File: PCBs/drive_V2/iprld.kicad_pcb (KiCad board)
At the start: 2 copper layers, 100 x 100 mm, 87 parts, among them IC1 W25Q16JVUXIQ_TR, IC2 ADS1115IDGSR, J1 TYPE-C-31-M-12, U1 AMS1117-3.3, U11 4N35, U12 4N35, U13 4N35, U14 4N35, U2 ESP32-S3, U3 4N35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

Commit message: fixed merge issues
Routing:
- net GND: track 251.2 -> 248.9 mm, vias 45 -> 44

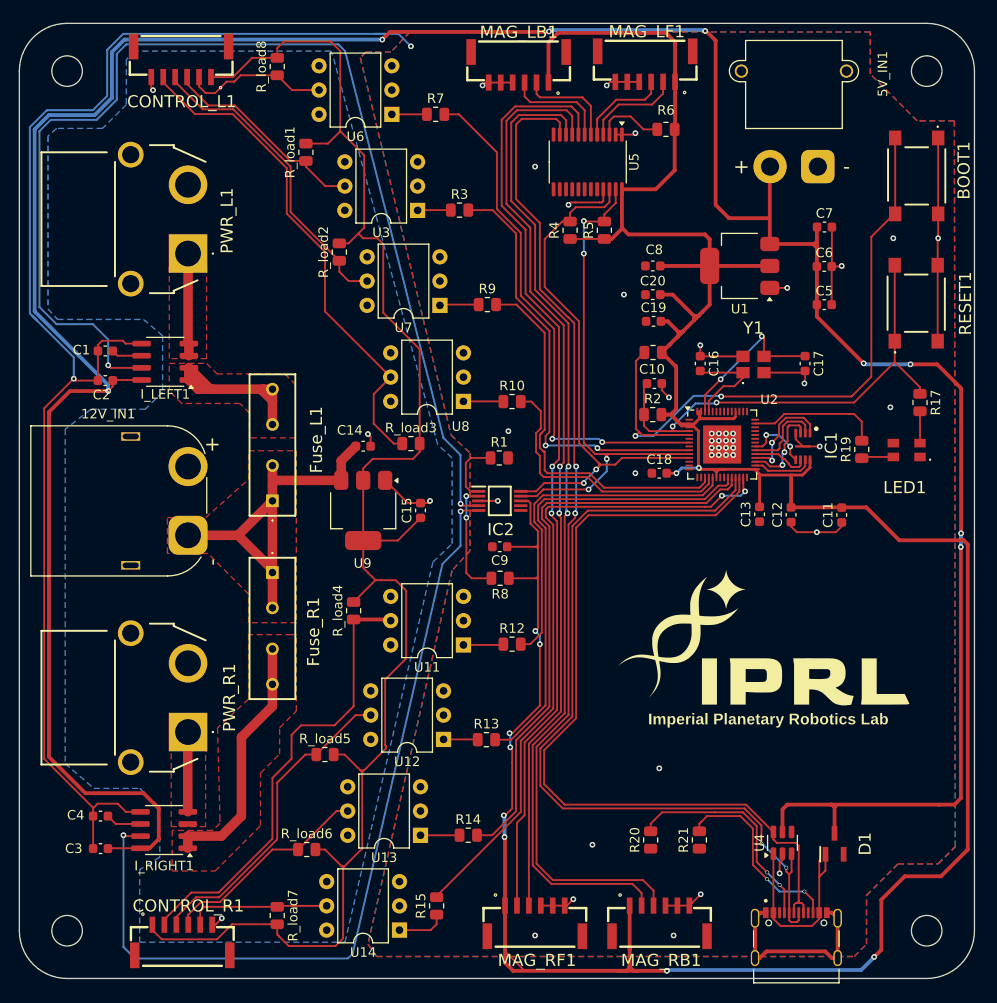
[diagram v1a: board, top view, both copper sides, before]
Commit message: added potential divider for I_OUT signals
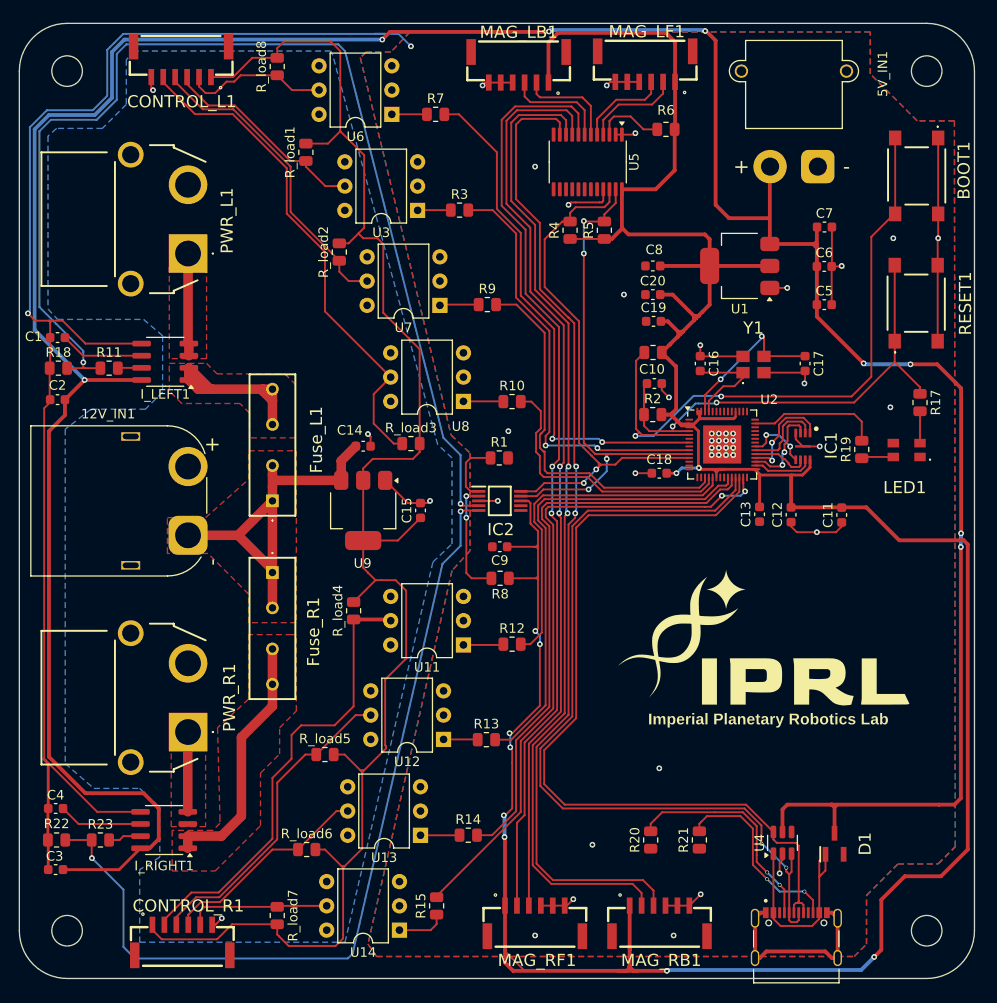
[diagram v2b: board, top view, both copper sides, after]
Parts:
- added R11: 5.1k, Resistor_SMD:R_0805_2012Metric, F.Cu at (9.40, 36.1)
- added R18: 10k, Resistor_SMD:R_0805_2012Metric, F.Cu at (4.09, 36.1)
- added R22: 10k, Resistor_SMD:R_0805_2012Metric, F.Cu at (3.90, 85.5)
- added R23: 5.1k, Resistor_SMD:R_0805_2012Metric, F.Cu at (8.49, 85.5)
- moved C2 5.39 mm to (4.00, 39.4)
- moved C1 5.19 mm to (4.00, 32.9)
- moved C3 5.19 mm to (3.80, 88.6)
- moved C4 4.77 mm to (3.80, 82.2)
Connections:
- IC1 pad 2: /SPIQ -> /SPID
- I_LEFT1 pad 7: /I_OUT_L -> Net-(I_LEFT1-VIOUT)
- I_RIGHT1 pad 7: /I_OUT_R -> Net-(I_RIGHT1-VIOUT)
- U2 pad 34: /SPIQ -> /SPID
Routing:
- net /SPIQ: track 8.65 -> 0.00 mm
- net /SPID: track 6.77 -> 15.4 mm
- net GND: track 248.9 -> 255.9 mm
- net Net-(I_LEFT1-FILTER): track 3.23 -> 8.81 mm
- net Net-(I_RIGHT1-FILTER): track 3.75 -> 8.78 mm
- net Net-(I_RIGHT1-VIOUT): track 0.00 -> 3.45 mm
- net +5V: track 352.8 -> 355.7 mm
- net /I_OUT_L: track 81.8 -> 79.0 mm
- net Net-(I_LEFT1-VIOUT): track 0.00 -> 2.50 mm
- net /I_OUT_R: track 46.5 -> 48.3 mm

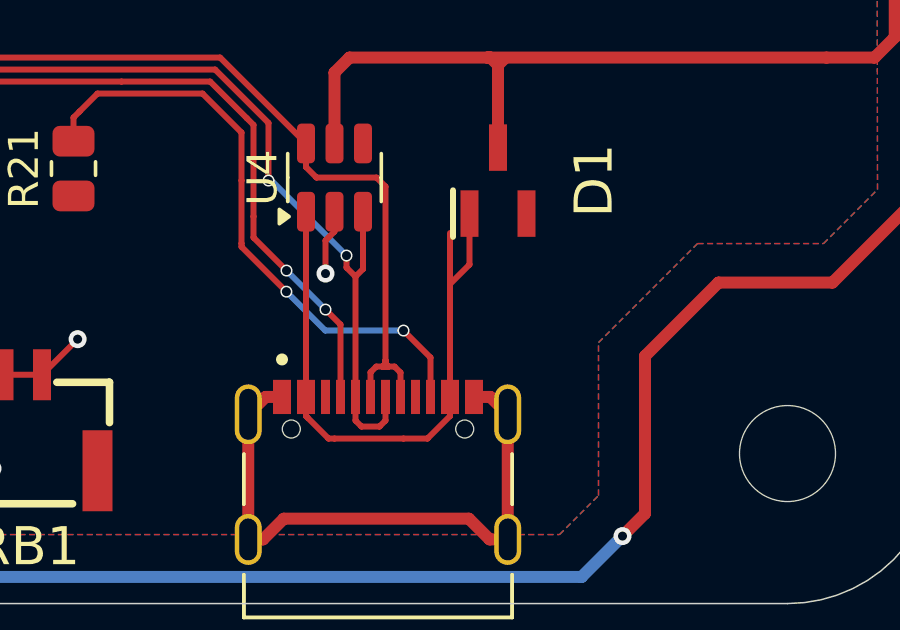
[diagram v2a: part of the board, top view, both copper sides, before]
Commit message: readded Diode D1, fixed connection issue with SPID and SPIQ
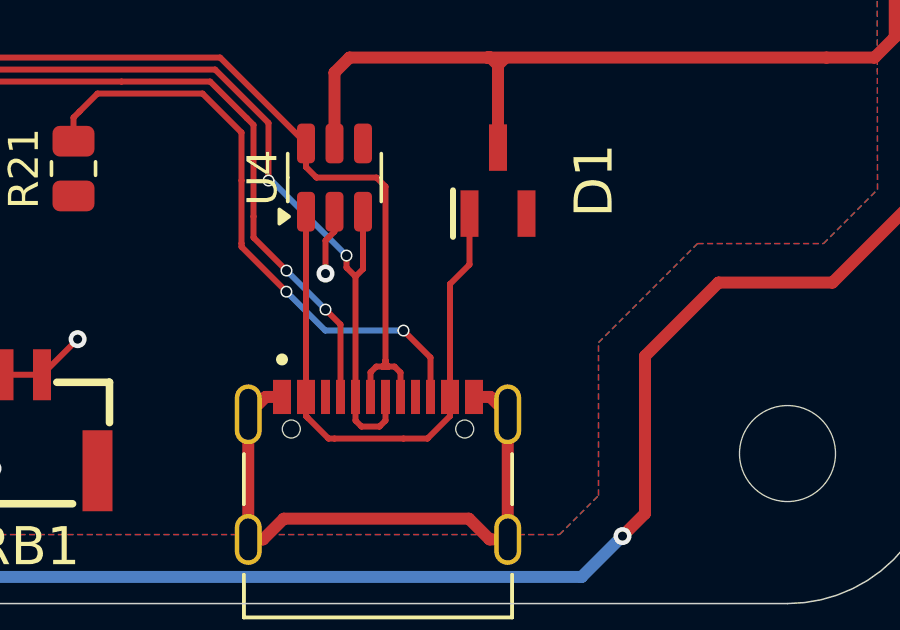
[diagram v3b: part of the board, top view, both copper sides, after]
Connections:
- IC1 pad 2: /SPID -> /SPIQ
- U2 pad 34: /SPID -> /SPIQ
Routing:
- net /SPIQ: track 0.00 -> 8.65 mm
- net /SPID: track 15.4 -> 6.77 mm
- net /VBUS: track 21.0 -> 19.3 mm
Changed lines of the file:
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@@
 	(net 125 "Net-(J1-CC2)")
 	(net 126 "Net-(I_RIGHT1-VIOUT)")
+	(net 127 "/SPIQ")
 	(footprint "Resistor_SMD:R_0805_2012Metric"
 		(layer "F.Cu")
@@
 			(layers "F.Cu" "F.Paste" "F.Mask")
 			(roundrect_rratio 0.25)
-			(net 18 "/SPID")
+			(net 127 "/SPIQ")
 			(pinfunction "SPIQ")
 			(pintype "bidirectional")
@@
 			(size 0.3 0.9)
 			(layers "F.Cu" "F.Paste" "F.Mask")
-			(net 18 "/SPID")
+			(net 127 "/SPIQ")
 			(pinfunction "DO(IO1)")
 			(pintype "passive")
@@
 		(tags "resistor")
 		(property "Reference" "R22"
-			(at 0 1.7 360)
+			(at 0 1.7 0)
 			(layer "F.SilkS")
 			(effects
@@
 		)
 		(property "Value" "10k"
-			(at 0 1.65 360)
+			(at 0 1.65 0)
 			(layer "F.Fab")
 			(effects
@@
 		)
 		(fp_text user "${REFERENCE}"
-			(at 0 0 360)
+			(at 0 0 0)
 			(layer "F.Fab")
 			(effects
@@
 		(tags "resistor")
 		(property "Reference" "R11"
-			(at 0 -1.65 360)
+			(at 0 -1.65 0)
 			(layer "F.SilkS")
 			(effects
@@
 		)
 		(property "Value" "5.1k"
-			(at 0 1.65 360)
+			(at 0 1.65 0)
 			(layer "F.Fab")
 			(effects
@@
 		)
 		(fp_text user "${REFERENCE}"
-			(at 0 0 360)
+			(at 0 0 0)
 			(layer "F.Fab")
 			(effects
@@
 	)
 	(segment
-		(start 83 94.5)
-		(end 82.2 94.5)
+		(start 83.75 89.35)
+		(end 83.75 93.1125)
 		(width 0.2)
 		(layer "F.Cu")
@@
 	)
 	(segment
-		(start 83.75 87.65)
-		(end 83.75 93.1125)
+		(start 83 94.5)
+		(end 82.2 94.5)
 		(width 0.2)
 		(layer "F.Cu")
@@
 	)
 	(segment
-		(start 78.903185 44.69375)
-		(end 77.0375 44.69375)
-		(width 0.2)
-		(layer "F.Cu")
-		(net 18)
-	)
-	(segment
-		(start 81.9375 41.69375)
-		(end 80.423286 41.69375)
-		(width 0.2)
-		(layer "F.Cu")
-		(net 18)
-	)
-	(segment
-		(start 79.6 44.5)
-		(end 79.4 44.7)
-		(width 0.2)
-		(layer "F.Cu")
-		(net 18)
-	)
-	(segment
-		(start 79.9375 42.179535)
-		(end 79.9375 43.660783)
-		(width 0.2)
-		(layer "F.Cu")
-		(net 18)
-	)
-	(segment
 		(start 80.712498 45.118748)
 		(end 81.2875 45.69375)
@@
 	)
 	(segment
-		(start 79.6 43.998283)
-		(end 79.6 44.5)
-		(width 0.2)
-		(layer "F.Cu")
-		(net 18)
-	)
-	(segment
 		(start 77.80625 44.29375)
 		(end 78.2 43.9)
@@
 	)
 	(segment
-		(start 82.2875 42.89375)
-		(end 82.2875 42.04375)
-		(width 0.2)
-		(layer "F.Cu")
-		(net 18)
-	)
-	(segment
-		(start 80.058518 42.058518)
-		(end 79.9375 42.179535)
-		(width 0.2)
-		(layer "F.Cu")
-		(net 18)
-	)
-	(segment
-		(start 78.909435 44.7)
-		(end 78.903185 44.69375)
-		(width 0.2)
-		(layer "F.Cu")
-		(net 18)
-	)
-	(segment
-		(start 79.4 44.7)
-		(end 78.909435 44.7)
-		(width 0.2)
-		(layer "F.Cu")
-		(net 18)
-	)
-	(segment
-		(start 82.2875 42.04375)
-		(end 81.9375 41.69375)
-		(width 0.2)
-		(layer "F.Cu")
-		(net 18)
-	)
-	(segment
 		(start 78.2 43.9)
 		(end 78.2 43.1)
@@
 	)
 	(segment
-		(start 79.9375 43.660783)
-		(end 79.6 43.998283)
-		(width 0.2)
-		(layer "F.Cu")
-		(net 18)
-	)
-	(segment
 		(start 80.712498 44.3)
 		(end 80.712498 45.118748)
@@
 		(net 18)
 	)
-	(segment
-		(start 80.423286 41.69375)
-		(end 80.058518 42.058518)
-		(width 0.2)
-		(layer "F.Cu")
-		(net 18)
-	)
 	(via
 		(at 80.712498 44.3)
@@
 		(net 126)
 	)
+	(segment
+		(start 78.903185 44.69375)
+		(end 77.0375 44.69375)
+		(width 0.2)
+		(layer "F.Cu")
+		(net 127)
+	)
+	(segment
+		(start 81.9375 41.69375)
+		(end 80.423286 41.69375)
+		(width 0.2)
+		(layer "F.Cu")
+		(net 127)
+	)
+	(segment
+		(start 79.6 44.5)
+		(end 79.4 44.7)
+		(width 0.2)
+		(layer "F.Cu")
+		(net 127)
+	)
+	(segment
+		(start 79.9375 42.179535)
+		(end 79.9375 43.660783)
+		(width 0.2)
+		(layer "F.Cu")
+		(net 127)
+	)
+	(segment
+		(start 79.6 43.998283)
+		(end 79.6 44.5)
+		(width 0.2)
+		(layer "F.Cu")
+		(net 127)
+	)
+	(segment
+		(start 82.2875 42.89375)
+		(end 82.2875 42.04375)
+		(width 0.2)
+		(layer "F.Cu")
+		(net 127)
+	)
+	(segment
+		(start 80.058518 42.058518)
+		(end 79.9375 42.179535)
+		(width 0.2)
+		(layer "F.Cu")
+		(net 127)
+	)
+	(segment
+		(start 78.909435 44.7)
+		(end 78.903185 44.69375)
+		(width 0.2)
+		(layer "F.Cu")
+		(net 127)
+	)
+	(segment
+		(start 79.4 44.7)
+		(end 78.909435 44.7)
+		(width 0.2)
+		(layer "F.Cu")
+		(net 127)
+	)
+	(segment
+		(start 82.2875 42.04375)
+		(end 81.9375 41.69375)
+		(width 0.2)
+		(layer "F.Cu")
+		(net 127)
+	)
+	(segment
+		(start 79.9375 43.660783)
+		(end 79.6 43.998283)
+		(width 0.2)
+		(layer "F.Cu")
+		(net 127)
+	)
+	(segment
+		(start 80.423286 41.69375)
+		(end 80.058518 42.058518)
+		(width 0.2)
+		(layer "F.Cu")
+		(net 127)
+	)
 	(zone

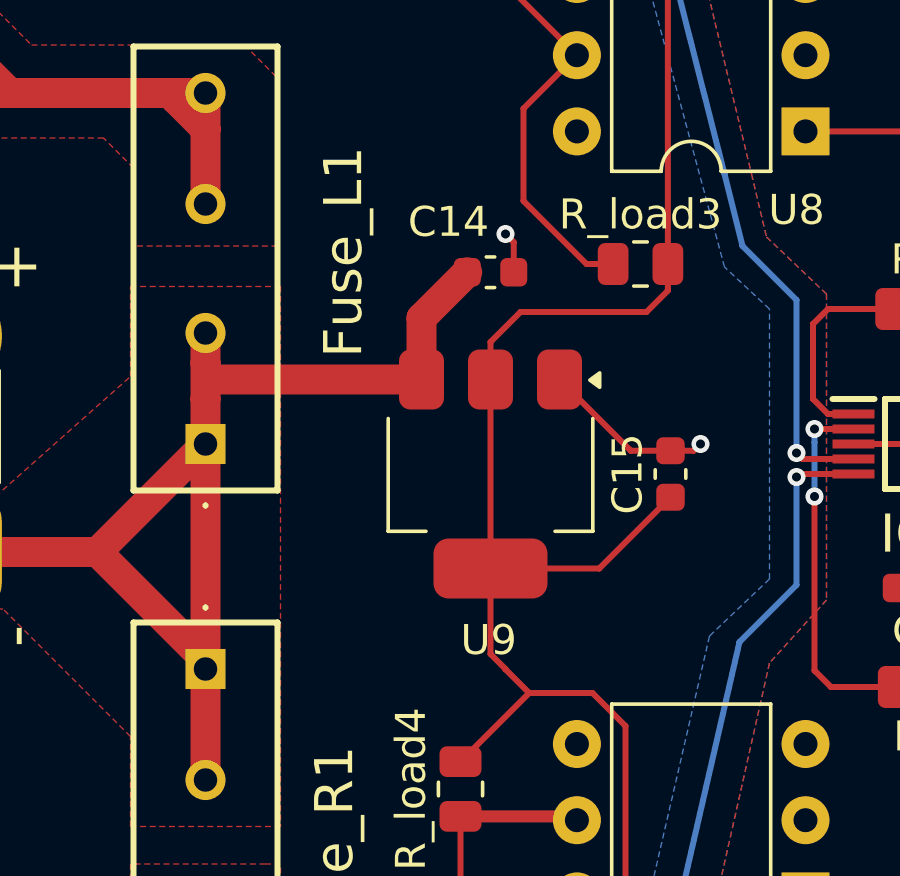
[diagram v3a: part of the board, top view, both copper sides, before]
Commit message: Switched the LDO to LM317
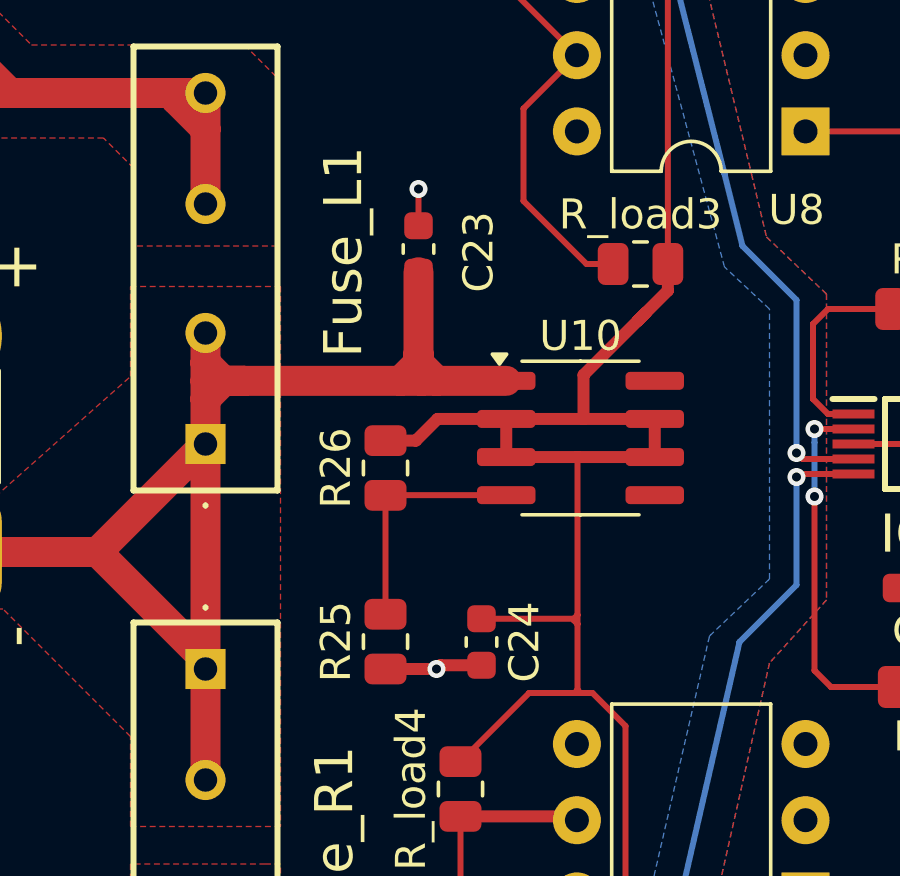
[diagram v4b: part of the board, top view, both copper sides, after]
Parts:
- removed C14, C15: 10u, Capacitor_SMD:C_0603_1608Metric
- removed U9: AMS1117-5.0, Package_TO_SOT_SMD:SOT-223-3_TabPin2
- added C23: 0.1u, Capacitor_SMD:C_0603_1608Metric, F.Cu at (33.6, 43.5)
- added C24: 1u, Capacitor_SMD:C_0603_1608Metric, F.Cu at (35.7, 56.6)
- added R25: 720, Resistor_SMD:R_0805_2012Metric, F.Cu at (32.5, 56.6)
- added R26: 240, Resistor_SMD:R_0805_2012Metric, F.Cu at (32.5, 50.8)
- added U10: LM317L_SO8, Package_SO:SOIC-8_3.9x4.9mm_P1.27mm, F.Cu at (39.0, 49.8)
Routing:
- net /+5V_ISO: track 173.0 -> 182.4 mm
- net Net-(U10-ADJ): track 0.00 -> 7.99 mm
- net +12V: track 43.1 -> 50.3 mm
- net GNDPWR: track 9.91 -> 7.22 mm

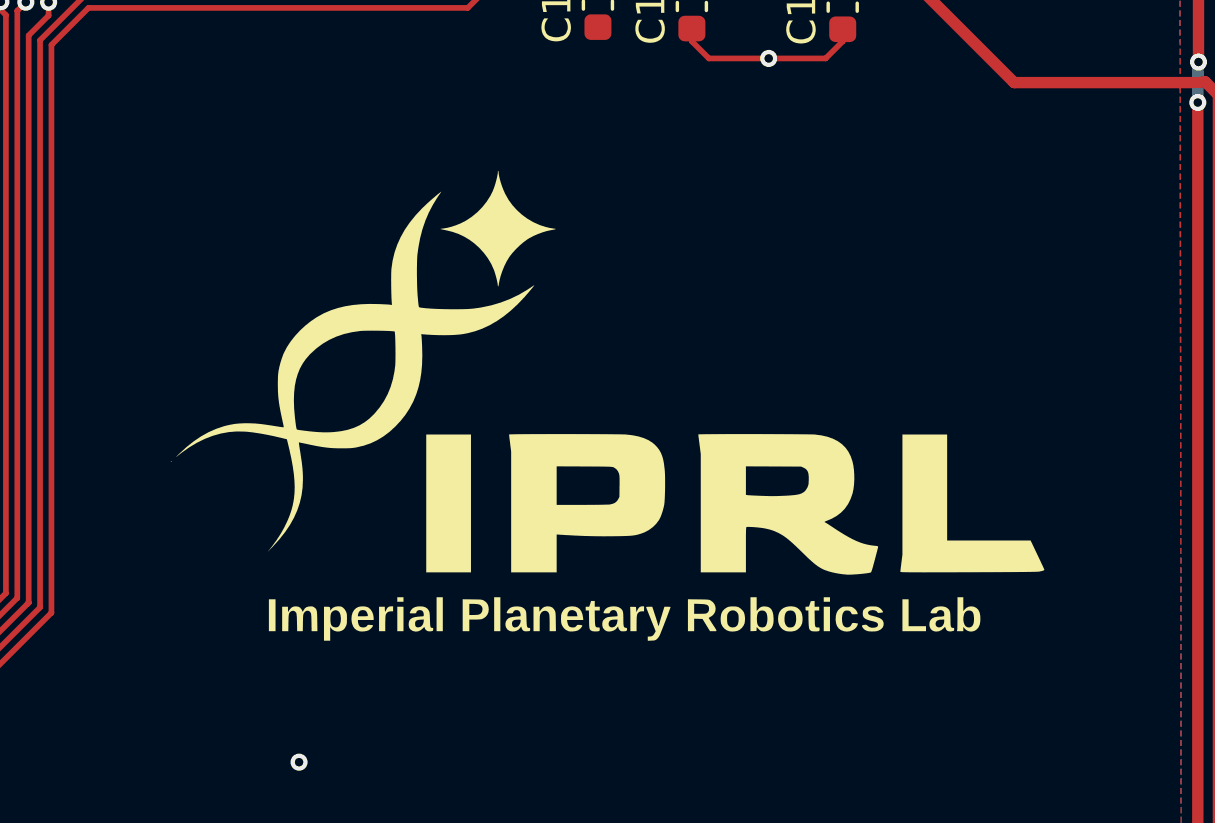
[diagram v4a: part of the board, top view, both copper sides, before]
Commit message: Manufacturing data created + added names to PCBs.
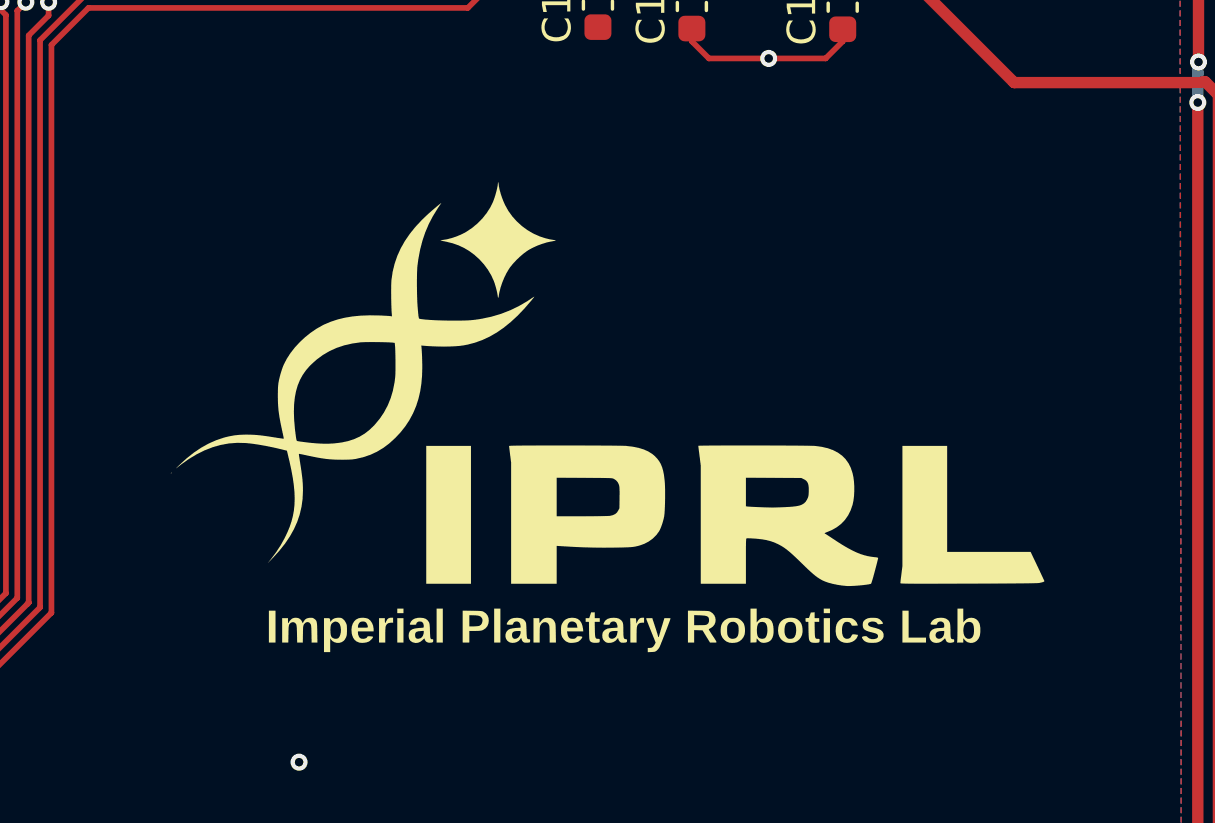
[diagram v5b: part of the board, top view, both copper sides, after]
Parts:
- moved G*** 0.40 mm to (78.0, 66.0)
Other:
- board text added: "Drive Board"
- board text added: "Maciej Grzegorczyk"
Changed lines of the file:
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@@
 			(plotinvisibletext no)
 			(sketchpadsonfab no)
-			(subtractmaskfromsilk no)
+			(subtractmaskfromsilk yes)
 			(outputformat 1)
 			(mirror no)
-			(drillshape 1)
+			(drillshape 0)
 			(scaleselection 1)
-			(outputdirectory "")
+			(outputdirectory "output/")
 		)
 	)
@@
 	(footprint "main_lib:IPRL_31mm"
 		(layer "F.Cu")
-		(at 78 65.6)
+		(at 78 66)
 		(property "Reference" "G***"
 			(at 0 0 0)
@@
 		(layer "Edge.Cuts")
 	)
+	(gr_text "Maciej Grzegorczyk"
+		(at 82 71 -0)
+		(layer "B.SilkS")
+		(effects
+			(font
+				(size 1.5 1.5)
+				(thickness 0.3)
+				(bold yes)
+			)
+			(justify left bottom mirror)
+		)
+	)
+	(gr_text "Drive Board\n"
+		(at 95 66 0)
+		(layer "B.SilkS" knockout)
+		(effects
+			(font
+				(size 5 5)
+				(thickness 0.75)
+			)
+			(justify left bottom mirror)
+		)
+	)
 	(segment
